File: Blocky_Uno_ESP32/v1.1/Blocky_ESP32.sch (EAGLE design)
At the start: 50 parts, among them Q2 S8050, Q3 DMG3415U, Q6 S8050, U1 ESP-WROOM-32, U2 AP2112-3.3, U5 MCP73831T-2ACI/OT, U6 CH340C, X1 JSTPH

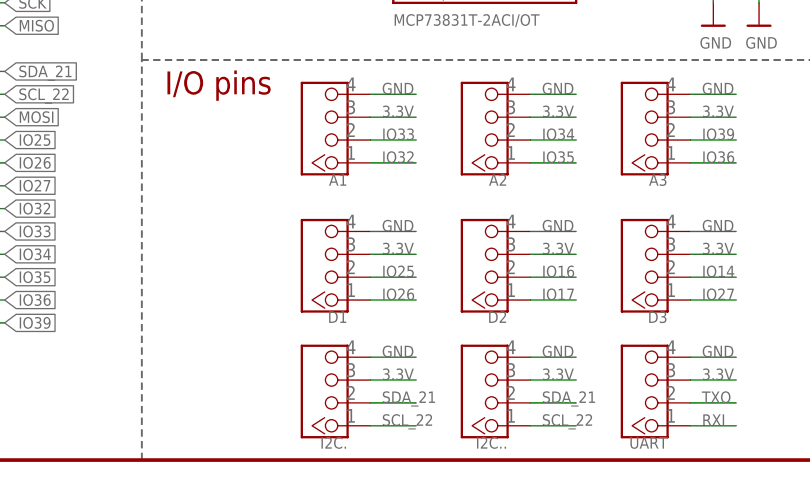
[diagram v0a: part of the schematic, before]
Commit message: Update pinout for Uno ESP32
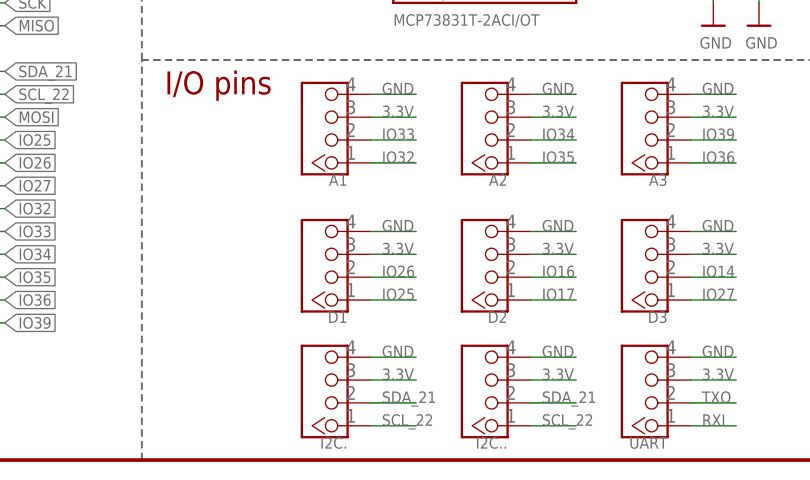
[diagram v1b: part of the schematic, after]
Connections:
- net IO25: now also D1.1; no longer D1.2
- net IO26: now also D1.2; no longer D1.1
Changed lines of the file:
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@@
 <grid distance="50" unitdist="mil" unit="mil" style="lines" multiple="1" display="no" altdistance="25" altunitdist="mil" altunit="mil"/>
 <layers>
-<layer number="1" name="Top" color="4" fill="1" visible="yes" active="no"/>
-<layer number="2" name="Route2" color="1" fill="3" visible="yes" active="no"/>
-<layer number="3" name="Route3" color="4" fill="3" visible="yes" active="no"/>
-<layer number="4" name="Route4" color="1" fill="4" visible="yes" active="no"/>
-<layer number="5" name="Route5" color="4" fill="4" visible="yes" active="no"/>
-<layer number="6" name="Route6" color="1" fill="8" visible="yes" active="no"/>
-<layer number="7" name="Route7" color="4" fill="8" visible="yes" active="no"/>
-<layer number="8" name="Route8" color="1" fill="2" visible="yes" active="no"/>
-<layer number="9" name="Route9" color="4" fill="2" visible="yes" active="no"/>
-<layer number="10" name="Route10" color="1" fill="7" visible="yes" active="no"/>
-<layer number="11" name="Route11" color="4" fill="7" visible="yes" active="no"/>
-<layer number="12" name="Route12" color="1" fill="5" visible="yes" active="no"/>
-<layer number="13" name="Route13" color="4" fill="5" visible="yes" active="no"/>
-<layer number="14" name="Route14" color="1" fill="6" visible="yes" active="no"/>
-<layer number="15" name="Route15" color="4" fill="6" visible="yes" active="no"/>
-<layer number="16" name="Bottom" color="1" fill="1" visible="yes" active="no"/>
-<layer number="17" name="Pads" color="2" fill="1" visible="yes" active="no"/>
-<layer number="18" name="Vias" color="2" fill="1" visible="yes" active="no"/>
-<layer number="19" name="Unrouted" color="6" fill="1" visible="yes" active="no"/>
-<layer number="20" name="Dimension" color="5" fill="1" visible="yes" active="no"/>
-<layer number="21" name="tPlace" color="7" fill="1" visible="yes" active="no"/>
-<layer number="22" name="bPlace" color="3" fill="1" visible="yes" active="no"/>
-<layer number="23" name="tOrigins" color="15" fill="1" visible="yes" active="no"/>
-<layer number="24" name="bOrigins" color="3" fill="1" visible="yes" active="no"/>
-<layer number="25" name="tNames" color="7" fill="1" visible="yes" active="no"/>
-<layer number="26" name="bNames" color="3" fill="1" visible="yes" active="no"/>
-<layer number="27" name="tValues" color="7" fill="1" visible="yes" active="no"/>
-<layer number="28" name="bValues" color="7" fill="1" visible="yes" active="no"/>
+<layer number="1" name="Top" color="4" fill="1" visible="no" active="no"/>
+<layer number="2" name="Route2" color="1" fill="3" visible="no" active="no"/>
+<layer number="3" name="Route3" color="4" fill="3" visible="no" active="no"/>
+<layer number="4" name="Route4" color="1" fill="4" visible="no" active="no"/>
+<layer number="5" name="Route5" color="4" fill="4" visible="no" active="no"/>
+<layer number="6" name="Route6" color="1" fill="8" visible="no" active="no"/>
+<layer number="7" name="Route7" color="4" fill="8" visible="no" active="no"/>
+<layer number="8" name="Route8" color="1" fill="2" visible="no" active="no"/>
+<layer number="9" name="Route9" color="4" fill="2" visible="no" active="no"/>
+<layer number="10" name="Route10" color="1" fill="7" visible="no" active="no"/>
+<layer number="11" name="Route11" color="4" fill="7" visible="no" active="no"/>
+<layer number="12" name="Route12" color="1" fill="5" visible="no" active="no"/>
+<layer number="13" name="Route13" color="4" fill="5" visible="no" active="no"/>
+<layer number="14" name="Route14" color="1" fill="6" visible="no" active="no"/>
+<layer number="15" name="Route15" color="4" fill="6" visible="no" active="no"/>
+<layer number="16" name="Bottom" color="1" fill="1" visible="no" active="no"/>
+<layer number="17" name="Pads" color="2" fill="1" visible="no" active="no"/>
+<layer number="18" name="Vias" color="2" fill="1" visible="no" active="no"/>
+<layer number="19" name="Unrouted" color="6" fill="1" visible="no" active="no"/>
+<layer number="20" name="Dimension" color="5" fill="1" visible="no" active="no"/>
+<layer number="21" name="tPlace" color="7" fill="1" visible="no" active="no"/>
+<layer number="22" name="bPlace" color="3" fill="1" visible="no" active="no"/>
+<layer number="23" name="tOrigins" color="15" fill="1" visible="no" active="no"/>
+<layer number="24" name="bOrigins" color="3" fill="1" visible="no" active="no"/>
+<layer number="25" name="tNames" color="7" fill="1" visible="no" active="no"/>
+<layer number="26" name="bNames" color="3" fill="1" visible="no" active="no"/>
+<layer number="27" name="tValues" color="7" fill="1" visible="no" active="no"/>
+<layer number="28" name="bValues" color="7" fill="1" visible="no" active="no"/>
 <layer number="29" name="tStop" color="7" fill="3" visible="no" active="no"/>
 <layer number="30" name="bStop" color="3" fill="6" visible="no" active="no"/>
@@
 <layer number="35" name="tGlue" color="7" fill="4" visible="no" active="no"/>
 <layer number="36" name="bGlue" color="3" fill="5" visible="no" active="no"/>
-<layer number="37" name="tTest" color="7" fill="1" visible="yes" active="no"/>
-<layer number="38" name="bTest" color="3" fill="1" visible="yes" active="no"/>
+<layer number="37" name="tTest" color="7" fill="1" visible="no" active="no"/>
+<layer number="38" name="bTest" color="3" fill="1" visible="no" active="no"/>
 <layer number="39" name="tKeepout" color="4" fill="11" visible="no" active="no"/>
 <layer number="40" name="bKeepout" color="1" fill="11" visible="no" active="no"/>
@@
 <layer number="44" name="Drills" color="7" fill="1" visible="no" active="no"/>
 <layer number="45" name="Holes" color="7" fill="1" visible="no" active="no"/>
-<layer number="46" name="Milling" color="3" fill="1" visible="yes" active="no"/>
-<layer number="47" name="Measures" color="7" fill="1" visible="yes" active="no"/>
-<layer number="48" name="Document" color="7" fill="1" visible="yes" active="no"/>
-<layer number="49" name="Reference" color="7" fill="1" visible="yes" active="no"/>
-<layer number="50" name="dxf" color="7" fill="1" visible="yes" active="no"/>
-<layer number="51" name="tDocu" color="7" fill="1" visible="yes" active="no"/>
-<layer number="52" name="bDocu" color="7" fill="1" visible="yes" active="no"/>
-<layer number="53" name="tGND_GNDA" color="7" fill="9" visible="yes" active="no"/>
-<layer number="54" name="bGND_GNDA" color="1" fill="9" visible="yes" active="no"/>
-<layer number="56" name="wert" color="7" fill="1" visible="yes" active="no"/>
-<layer number="57" name="tCAD" color="7" fill="1" visible="yes" active="no"/>
-<layer number="58" name="bCAD" color="11" fill="1" visible="yes" active="no"/>
-<layer number="59" name="tCarbon" color="7" fill="1" visible="yes" active="no"/>
-<layer number="60" name="bCarbon" color="7" fill="1" visible="yes" active="no"/>
+<layer number="46" name="Milling" color="3" fill="1" visible="no" active="no"/>
+<layer number="47" name="Measures" color="7" fill="1" visible="no" active="no"/>
+<layer number="48" name="Document" color="7" fill="1" visible="no" active="no"/>
+<layer number="49" name="Reference" color="7" fill="1" visible="no" active="no"/>
+<layer number="50" name="dxf" color="7" fill="1" visible="no" active="no"/>
+<layer number="51" name="tDocu" color="7" fill="1" visible="no" active="no"/>
+<layer number="52" name="bDocu" color="7" fill="1" visible="no" active="no"/>
+<layer number="53" name="tGND_GNDA" color="7" fill="9" visible="no" active="no"/>
+<layer number="54" name="bGND_GNDA" color="1" fill="9" visible="no" active="no"/>
+<layer number="56" name="wert" color="7" fill="1" visible="no" active="no"/>
+<layer number="57" name="tCAD" color="7" fill="1" visible="no" active="no"/>
+<layer number="58" name="bCAD" color="11" fill="1" visible="no" active="no"/>
+<layer number="59" name="tCarbon" color="7" fill="1" visible="no" active="no"/>
+<layer number="60" name="bCarbon" color="7" fill="1" visible="no" active="no"/>
 <layer number="88" name="SimResults" color="9" fill="1" visible="yes" active="yes"/>
 <layer number="89" name="SimProbes" color="9" fill="1" visible="yes" active="yes"/>
@@
 </segment>
 <segment>
-<pinref part="D1" gate="G$1" pin="2"/>
-<wire x1="378.46" y1="15.24" x2="383.54" y2="15.24" width="0.1524" layer="91"/>
-<label x="379.73" y="15.24" size="1.27" layer="95" ratio="10"/>
+<pinref part="D1" gate="G$1" pin="1"/>
+<wire x1="378.46" y1="12.7" x2="383.54" y2="12.7" width="0.1524" layer="91"/>
+<label x="379.73" y="12.7" size="1.27" layer="95" ratio="10"/>
 </segment>
 </net>
@@
 </segment>
 <segment>
-<pinref part="D1" gate="G$1" pin="1"/>
-<wire x1="378.46" y1="12.7" x2="383.54" y2="12.7" width="0.1524" layer="91"/>
-<label x="379.73" y="12.7" size="1.27" layer="95" ratio="10"/>
-</segment>
-</net>
+<pinref part="D1" gate="G$1" pin="2"/>
+<wire x1="378.46" y1="15.24" x2="383.54" y2="15.24" width="0.1524" layer="91"/>
+<label x="379.73" y="15.24" size="1.27" layer="95" ratio="10"/>
+</segment>
+</net>
